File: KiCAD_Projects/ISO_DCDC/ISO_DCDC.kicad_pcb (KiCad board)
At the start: 2 copper layers, 100 x 120 mm, 74 parts, among them IC1 PC817, IC2 PC817, IC3 PC817, IC4 PC817, IC5 PC817, P1 CONN_01X01, P10 CONN_01X02, P11 CONN_01X02, P12 CONN_01X01, P13 CONN_01X04, P14 CONN_01X02, P15 CONN_01X02, P16 CONN_01X02, P19 CONN_01X01, P2 CONN_01X01, P20 CONN_01X01, P21 CONN_01X02, P22 CONN_01X01, P23 CONN_01X01, P25 CONN_01X01, P26 CONN_01X01, P3 CONN_01X01, P30 CONN_01X01, P4 CONN_01X02, P5 CONN_01X02, P6 CONN_01X04, P7 CONN_01X04, P8 CONN_01X01, P9 CONN_01X01, Q1 MOSFET_N, U1 V23076-D3001-D142, U2 V23076-D3001-D142, U3 V23076-D3001-D142

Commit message: no message
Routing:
- net +BATT: track 21.7 -> 53.5 mm
- net Net-(P30-Pad1): track 0.00 -> 10.0 mm
- net Net-(C3-Pad1): track 28.5 -> 30.7 mm
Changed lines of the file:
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@@
   (general
     (links 131)
-    (no_connects 3)
+    (no_connects 0)
     (area -0.075001 -0.075001 100.075001 120.075001)
     (thickness 1.6)
     (drawings 8)
-    (tracks 343)
+    (tracks 351)
     (zones 0)
     (modules 74)
@@
   )
   (setup
-    (last_trace_width 0.5)
+    (last_trace_width 0.25)
     (user_trace_width 0.5)
     (user_trace_width 1)
@@
   (segment (start 7 50.5) (end 7 43) (width 0.5) (layer B.Cu) (net 1))
   (segment (start 8.5 52) (end 7 50.5) (width 0.5) (layer B.Cu) (net 1))
+  (segment (start 20.8 59) (end 26.5 64.7) (width 0.25) (layer B.Cu) (net 2) (status 400000))
+  (segment (start 20 74) (end 14 80) (width 0.25) (layer B.Cu) (net 2) (status 800000))
+  (segment (start 25.5 74) (end 20 74) (width 0.25) (layer B.Cu) (net 2))
+  (segment (start 26.5 73) (end 25.5 74) (width 0.25) (layer B.Cu) (net 2))
+  (segment (start 26.5 64.7) (end 26.5 73) (width 0.25) (layer B.Cu) (net 2))
   (segment (start 35.1 45.3) (end 35.1 38.1) (width 3) (layer B.Cu) (net 2))
   (segment (start 35.1 38.1) (end 30 33) (width 3) (layer B.Cu) (net 2))
@@
   (segment (start 14 80) (end 14 85) (width 0.5) (layer B.Cu) (net 2))
   (segment (start 14 85) (end 13 86) (width 0.5) (layer B.Cu) (net 2))
+  (segment (start 26.4 25) (end 26.4 22.89972) (width 2) (layer B.Cu) (net 3) (status C00000))
+  (segment (start 26.4 22.89972) (end 26.49988 22.79984) (width 2) (layer B.Cu) (net 3) (status C00000))
   (segment (start 13 26.9) (end 15.6 26.9) (width 2) (layer B.Cu) (net 3))
   (segment (start 15.6 26.9) (end 16 26.5) (width 2) (layer B.Cu) (net 3))
@@
   (segment (start 27.5 73.5) (end 27.5 60) (width 0.5) (layer B.Cu) (net 32))
   (segment (start 25 76) (end 27.5 73.5) (width 0.5) (layer B.Cu) (net 32))
+  (segment (start 25 12.5) (end 35 12.5) (width 0.25) (layer B.Cu) (net 33) (status C00000))
   (segment (start 59.70016 38.19952) (end 59.70016 23.80048) (width 0.5) (layer B.Cu) (net 34))
   (segment (start 67.29984 99.34874) (end 82.26126 99.34874) (width 0.5) (layer B.Cu) (net 35))

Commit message: no message
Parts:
- R3, R4: footprint RP_KiCAD_Libs:0204_2f5 -> RP_KiCAD_Libs:C1608_WP; moved to B.Cu
- moved R4 5.02 mm to (36.0, 22.5)
- moved P19 2.50 mm to (17.5, 36.0)
- moved D3 2.06 mm to (25.0, 32.5)
- moved R3 1.12 mm to (40.5, 21.5), turned to 0 degrees
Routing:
- net +BATT: track 53.5 -> 64.0 mm
- net GNDPWR: track 354.3 -> 362.4 mm
- net Net-(DCDC1-Pad4): track 12.7 -> 8.59 mm
- net /15V: track 164.3 -> 165.9 mm
- net Net-(D3-Pad1): track 5.74 -> 6.45 mm

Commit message: no message
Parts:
- removed P16: CONN_01X02, RP_KiCAD_Connector:XA_2T
- removed P30: CONN_01X01, Heatsinks:16PB017_16.25.16
- added C11: 470p, RP_KiCAD_Libs:C1608_WP, B.Cu at (52.0, 15.0)
- added C2: 0.22u, RP_KiCAD_Libs:C1608_WP, B.Cu at (43.0, 10.0)
- added C8: 470p, RP_KiCAD_Libs:C1608_WP, B.Cu at (52.0, 13.0)
- added D7: DIODE, RP_KiCAD_Libs:C3216, B.Cu at (38.5, 19.0)
- added R10: 100k, RP_KiCAD_Libs:C1608_WP, B.Cu at (49.5, 14.0)
- added R13: R, RP_KiCAD_Libs:0204_2f5, F.Cu at (59.5, 19.5)
- added R14: R, RP_KiCAD_Libs:C1608_WP, B.Cu at (73.0, 13.5)
- D2: footprint Diodes_ThroughHole:Diode_DO-201AD_Horizontal_RM15 -> Diodes_SMD:POWER_DI5; moved to B.Cu
- DCDC1: value SI-8008HFE -> SI-8010Y; footprint TO_SOT_Packages_THT:Pentawatt_Neutral_Staggered_Verical_TO220-5-T05D -> TO_SOT_Packages_THT:TO-220_7_Vertical
- IC1, IC2, IC3, IC4, IC5: footprint Opto-Devices:Optocoupler_SMD_HandSoldering_KPC357_LTV35x_PC357_SingleChannel -> Housings_SOIC:SOIJ-4_5.3x5.3mm_Pitch1.27mm
- L1: footprint Choke_Toroid_ThroughHole:Choke_Toroid_horizontal_Diameter26mm -> Choke_Toroid_ThroughHole:Choke_Toroid_8.5x24mm_Vertical
- R19: moved to F.Cu
- R3: value R -> 15k
- R4: value R -> 1k
- moved D4 50.1 mm to (74.5, 18.5), turned to 270 degrees
- moved P10 42.0 mm to (77.5, 28.5)
- moved R7 41.6 mm to (77.5, 21.0), turned to 0 degrees
- moved C9 40.0 mm to (70.0, 28.5)
- moved DCDC2 36.8 mm to (48.8, 35.6)
- moved R8 32.9 mm to (66.0, 46.5), turned to 270 degrees
- moved P15 31.6 mm to (86.5, 28.5)
- moved R11 31.2 mm to (36.0, 70.5), turned to 270 degrees
- moved IC3 29.8 mm to (59.0, 68.5)
- moved Q1 29.8 mm to (32.5, 70.5)
- moved R21 29.5 mm to (66.0, 72.0)
- moved R19 29.3 mm to (34.0, 70.5)
- moved D5 27.8 mm to (68.5, 43.0), turned to 180 degrees
- moved C5 27.5 mm to (54.0, 8.50), turned to 180 degrees
- moved C3 25.8 mm to (24.5, 9.00), turned to 90 degrees
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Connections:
- DCDC1 pad 1: Net-(C3-Pad1) -> Net-(C2-Pad2)
- DCDC1 pad 3: GNDPWR -> Net-(C3-Pad1)
- DCDC1 pad 4: Net-(DCDC1-Pad4) -> GNDPWR
- DCDC1 pad 5: Net-(C5-Pad2) -> Net-(C8-Pad1)
- IC1 pad 2: /12V_CAN_GND -> /5V_GND
- IC2 pad 2: /5V_GND -> /12V_CAN_GND
- IC4 pad 2: Net-(IC4-Pad2) -> /5V_GND
- IC5 pad 1: /POWER_EN_HIGH -> Net-(IC5-Pad1)
- IC5 pad 3: Net-(IC5-Pad3) -> /5V_GND
- P13 pad 1: Net-(P13-Pad1) -> /5V_GND
- P13 pad 2: Net-(IC4-Pad2) -> /5V
- P13 pad 3: Net-(IC5-Pad4) -> Net-(P13-Pad3)
- P13 pad 4: Net-(IC5-Pad3) -> Net-(IC5-Pad4)
- P21 pad 1: /POWER_EN_HIGH -> Net-(P21-Pad1)
- P21 pad 2: Net-(P21-Pad2) -> /15V
- P4 pad 2: Net-(P21-Pad2) -> Net-(P21-Pad1)
- P5 pad 1: Net-(P21-Pad2) -> Net-(P21-Pad1)
- R22 pad 1: Net-(P13-Pad1) -> Net-(P13-Pad3)
- R3 pad 1: Net-(DCDC1-Pad4) -> Net-(DCDC1-Pad6)
- R4 pad 2: Net-(DCDC1-Pad4) -> Net-(DCDC1-Pad6)
- R6 pad 1: /5V -> /12V_CAN
- R9 pad 1: /12V_CAN -> /5V
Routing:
- net GNDPWR: track 362.4 -> 301.6 mm
- net /12V_RasPi: track 90.4 -> 47.6 mm
- net /12V_RasPi_GND: track 82.8 -> 47.2 mm
- net Net-(IC4-Pad2): track 26.5 -> 0.00 mm
- net /5V: track 55.3 -> 81.1 mm
- net Net-(P13-Pad1): track 25.5 -> 0.00 mm
- net Net-(IC5-Pad3): track 24.5 -> 0.00 mm
- net Net-(IC2-Pad3): track 30.9 -> 9.23 mm
- net Net-(C3-Pad1): track 30.7 -> 49.9 mm
- net +BATT: track 64.0 -> 47.2 mm
- net Net-(DCDC1-Pad6): track 0.00 -> 13.9 mm
- net Net-(IC3-Pad3): track 78.1 -> 64.7 mm
- net /POWER_EN_HIGH: track 262.5 -> 275.7 mm
- net Net-(IC5-Pad4): track 24.5 -> 13.0 mm
- net /12V_CAN: track 78.9 -> 89.8 mm
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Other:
- board size 100 x 120 mm -> 90 x 100 mm

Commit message: no message
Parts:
- added JP1: JUMPER, Pin_Headers:Pin_Header_Straight_1x02, F.Cu at (79.0, 40.5)
- added JP2: JUMPER, Pin_Headers:Pin_Header_Straight_1x02, F.Cu at (81.5, 55.5)
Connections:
- P6 pad 3: Net-(P6-Pad3) -> Net-(JP1-Pad1)
- P6 pad 4: Net-(P6-Pad4) -> Net-(JP2-Pad1)
- P7 pad 3: Net-(P6-Pad3) -> Net-(JP1-Pad2)
- P7 pad 4: Net-(P6-Pad4) -> Net-(JP2-Pad2)
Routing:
- net Net-(P6-Pad3): track 22.7 -> 0.00 mm, vias 2 -> 0
- net Net-(JP2-Pad2): track 0.00 -> 20.7 mm, vias 0 -> 2
- net Net-(P6-Pad4): track 20.6 -> 0.00 mm, vias 2 -> 0
- net Net-(JP1-Pad1): track 0.00 -> 18.4 mm, vias 0 -> 2
- net Net-(JP1-Pad2): track 0.00 -> 6.29 mm
- net Net-(JP2-Pad1): track 0.00 -> 5.83 mm

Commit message: 3Dデータ組み合わてテスト
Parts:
- DCDC4: footprint RP_KiCAD_Libs:MGS30 -> Converters_DCDC_ACDC:MGS30

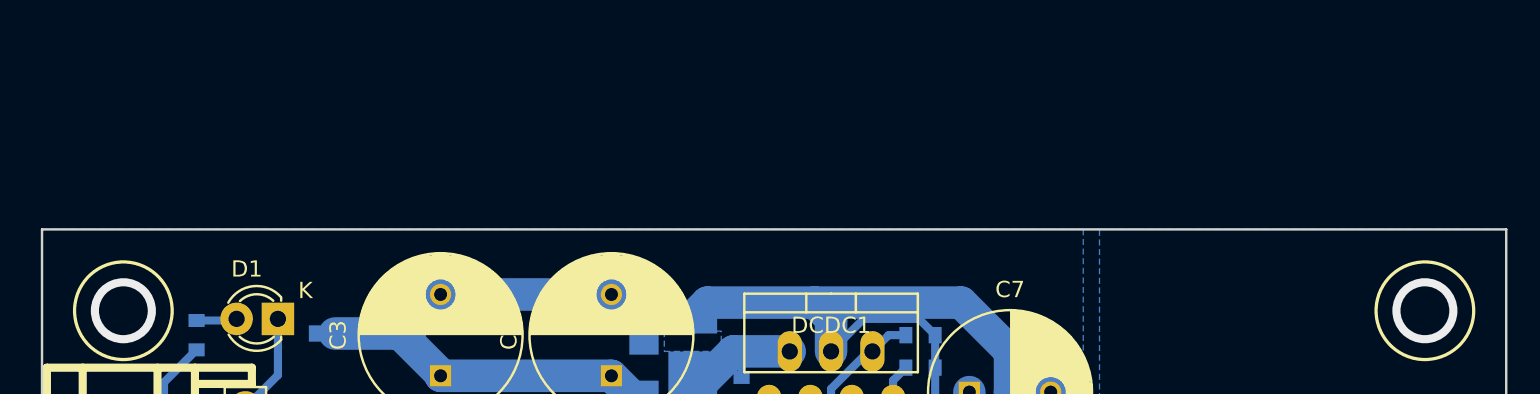
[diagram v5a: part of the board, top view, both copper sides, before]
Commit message: 4.0.5のライブラリを追加｡インダクタの3Dモジュール追加
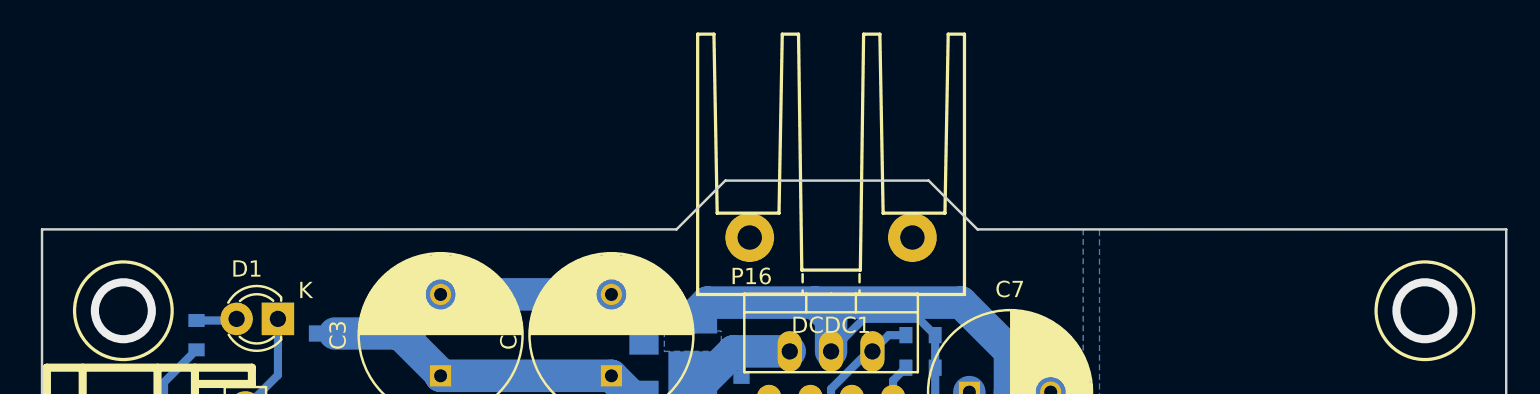
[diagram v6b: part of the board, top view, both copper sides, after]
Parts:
- added P16: TST, Heatsinks:16PB017_16.25.16, F.Cu at (48.5, 6.00)
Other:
- board size 90 x 100 mm -> 90 x 103 mm
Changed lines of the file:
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@@
-(kicad_pcb (version 4) (host pcbnew 4.0.4-stable)
+(kicad_pcb (version 4) (host pcbnew 4.0.5)
   (general
-    (links 144)
-    (no_connects 0)
+    (links 145)
+    (no_connects 1)
     (area -0.075001 -0.075001 90.075001 100.075001)
     (thickness 1.6)
-    (drawings 7)
+    (drawings 11)
     (tracks 437)
     (zones 0)
-    (modules 81)
-    (nets 50)
+    (modules 82)
+    (nets 51)
   )
   (page A4)
@@
   (net 48 "Net-(JP2-Pad1)")
   (net 49 "Net-(JP2-Pad2)")
+  (net 50 "Net-(P16-Pad1)")
   (net_class Default "これは標準のネット クラスです。"
     (clearance 0.2)
@@
     (add_net "Net-(JP2-Pad2)")
     (add_net "Net-(P13-Pad3)")
+    (add_net "Net-(P16-Pad1)")
     (add_net "Net-(P20-Pad1)")
     (add_net "Net-(P21-Pad1)")
@@
     )
   )
-  (module Choke_Toroid_ThroughHole:Choke_Toroid_8.5x24mm_Vertical (layer F.Cu)
-    (at 56 14 180)
-    (descr "Toroid, Coil, Choke,  8.5mm x 24mm, Vertical, Inductor, Drossel, Thruhole,")
-    (tags "Toroid, Coil, Choke,  8.5mm x 24mm, Vertical, Inductor, Drossel, Thruhole,")
-    (fp_text reference L1 (at 16.51 -10.16 180) (layer F.SilkS)
-      (effects (font (size 1 1) (thickness 0.15)))
-    )
-    (fp_text value "100uH 9A" (at 13 2 180) (layer F.Fab)
-      (effects (font (size 1 1) (thickness 0.15)))
-    )
-    (fp_line (start 0 0) (end 10 0) (layer F.SilkS) (width 0.2))
-    (fp_line (start 0 -7.5) (end 0 0) (layer F.SilkS) (width 0.2))
-    (fp_line (start 10 -7.5) (end 0 -7.5) (layer F.SilkS) (width 0.2))
-    (fp_line (start 13 0) (end 23 0) (layer F.SilkS) (width 0.2))
-    (fp_line (start 23 -7.5) (end 13 -7.5) (layer F.SilkS) (width 0.2))
-    (fp_line (start 23 -7.5) (end 23 0) (layer F.SilkS) (width 0.2))
-    (pad 1 thru_hole circle (at 11.5 0 180) (size 1.99898 1.99898) (drill 1) (layers *.Cu *.Mask F.SilkS)
-      (net 39 "Net-(C2-Pad1)"))
-    (pad 2 thru_hole circle (at 11.5 -7.5 180) (size 1.99898 1.99898) (drill 1) (layers *.Cu *.Mask F.SilkS)
-      (net 15 /15V))
-  )
   (module RP_KiCAD_Libs:0204_2f5 (layer F.Cu)
     (at 59.5 19.5 45)
@@
     )
   )
-  (gr_line (start 90 0) (end 0 0) (angle 90) (layer Edge.Cuts) (width 0.15))
+  (module Choke_Toroid_ThroughHole:Choke_Toroid_8.5x24mm_Vertical (layer F.Cu)
+    (at 56 14 180)
+    (descr "Toroid, Coil, Choke,  8.5mm x 24mm, Vertical, Inductor, Drossel, Thruhole,")
+    (tags "Toroid, Coil, Choke,  8.5mm x 24mm, Vertical, Inductor, Drossel, Thruhole,")
+    (fp_text reference L1 (at 16.51 -10.16 180) (layer F.SilkS)
+      (effects (font (size 1 1) (thickness 0.15)))
+    )
+    (fp_text value "100uH 9A" (at 13 2 180) (layer F.Fab)
+      (effects (font (size 1 1) (thickness 0.15)))
+    )
+    (fp_line (start 0 0) (end 10 0) (layer F.SilkS) (width 0.2))
+    (fp_line (start 0 -7.5) (end 0 0) (layer F.SilkS) (width 0.2))
+    (fp_line (start 10 -7.5) (end 0 -7.5) (layer F.SilkS) (width 0.2))
+    (fp_line (start 13 0) (end 23 0) (layer F.SilkS) (width 0.2))
+    (fp_line (start 23 -7.5) (end 13 -7.5) (layer F.SilkS) (width 0.2))
+    (fp_line (start 23 -7.5) (end 23 0) (layer F.SilkS) (width 0.2))
+    (pad 1 thru_hole circle (at 11.5 0 180) (size 1.99898 1.99898) (drill 1) (layers *.Cu *.Mask F.SilkS)
+      (net 39 "Net-(C2-Pad1)"))
+    (pad 2 thru_hole circle (at 11.5 -7.5 180) (size 1.99898 1.99898) (drill 1) (layers *.Cu *.Mask F.SilkS)
+      (net 15 /15V))
+    (model Choke_Toroid_ThroughHole.3dshapes/Choke_Toroid_11x25mm.wrl
+      (at (xyz 0.45 0.015 0.45))
+      (scale (xyz 0.37 0.37 0.37))
+      (rotate (xyz 90 0 0))
+    )
+  )
+  (module Heatsinks:16PB017_16.25.16 (layer F.Cu)
+    (at 48.5 6)
+    (fp_text reference P16 (at -4.9 -3.1) (layer F.SilkS)
+      (effects (font (size 1 1) (thickness 0.15)))
+    )
+    (fp_text value TST (at 4.9 -2.9) (layer F.Fab)
+      (effects (font (size 1 1) (thickness 0.15)))
+    )
+    (fp_line (start 1.8 -3.5) (end 2 -18) (layer F.SilkS) (width 0.2))
+    (fp_line (start -2 -18) (end -1.8 -3.5) (layer F.SilkS) (width 0.2))
+    (fp_line (start -7 -7) (end -3.2 -7) (layer F.SilkS) (width 0.2))
+    (fp_line (start 7 -7) (end 3.2 -7) (layer F.SilkS) (width 0.2))
+    (fp_line (start 7.2 -18) (end 7 -7) (layer F.SilkS) (width 0.2))
+    (fp_line (start 3 -18) (end 3.2 -7) (layer F.SilkS) (width 0.2))
+    (fp_line (start -3.2 -7) (end -3 -18) (layer F.SilkS) (width 0.2))
+    (fp_line (start -7.2 -18) (end -7 -7) (layer F.SilkS) (width 0.2))
+    (fp_line (start 2 -18) (end 3 -18) (layer F.SilkS) (width 0.2))
+    (fp_line (start -2 -18) (end -3 -18) (layer F.SilkS) (width 0.2))
+    (fp_line (start -1.8 -3.5) (end 1.8 -3.5) (layer F.SilkS) (width 0.2))
+    (fp_line (start 8.2 -18) (end 7.2 -18) (layer F.SilkS) (width 0.2))
+    (fp_line (start -8.2 -18) (end -7.2 -18) (layer F.SilkS) (width 0.2))
+    (fp_line (start -8.2 -2) (end -8.2 -18) (layer F.SilkS) (width 0.2))
+    (fp_line (start -8.2 -2) (end 8.2 -2) (layer F.SilkS) (width 0.2))
+    (fp_line (start 8.2 -2) (end 8.2 -18) (layer F.SilkS) (width 0.2))
+    (fp_line (start -1.75 -2.25) (end -1.75 -2) (layer F.SilkS) (width 0.15))
+    (fp_line (start 1.75 -2.25) (end 1.75 -2) (layer F.SilkS) (width 0.15))
+    (fp_line (start 1.75 -3.25) (end 1.75 -2.75) (layer F.SilkS) (width 0.15))
+    (fp_line (start -1.75 -3.25) (end -1.75 -2.75) (layer F.SilkS) (width 0.15))
+    (pad 1 thru_hole circle (at -5 -5.5) (size 3 3) (drill 1.5) (layers *.Cu *.Mask F.SilkS)
+      (net 50 "Net-(P16-Pad1)"))
+    (pad 1 thru_hole circle (at 5 -5.5) (size 3 3) (drill 1.5) (layers *.Cu *.Mask F.SilkS)
+      (net 50 "Net-(P16-Pad1)"))
+    (model Heatsinks/16PB017.wrl
+      (at (xyz 0 0.08 0))
+      (scale (xyz 3.9 3.9 3.9))
+      (rotate (xyz -90 0 0))
+    )
+  )
+  (gr_line (start 39 0) (end 0 0) (angle 90) (layer Edge.Cuts) (width 0.15))
+  (gr_line (start 57.5 0) (end 90 0) (angle 90) (layer Edge.Cuts) (width 0.15))
+  (gr_line (start 54.5 -3) (end 57.5 0) (angle 90) (layer Edge.Cuts) (width 0.15))
+  (gr_line (start 42 -3) (end 54.5 -3) (angle 90) (layer Edge.Cuts) (width 0.15))
+  (gr_line (start 39 0) (end 42 -3) (angle 90) (layer Edge.Cuts) (width 0.15))
   (gr_line (start 90 100) (end 90 0) (angle 90) (layer Edge.Cuts) (width 0.15))
   (gr_line (start 0 100) (end 90 100) (angle 90) (layer Edge.Cuts) (width 0.15))
@@
   (via (at 82 52.5) (size 1.5) (drill 0.8) (layers F.Cu B.Cu) (net 49))
   (segment (start 86.5 41) (end 85.5 41) (width 0.5) (layer B.Cu) (net 49))
-  (zone (net 1) (net_name GNDPWR) (layer B.Cu) (hatch edge 0.508)
-    (connect_pads yes (clearance 0.35))
-    (min_thickness 0.026)
-    (fill yes (arc_segments 16) (thermal_gap 0.508) (thermal_bridge_width 0.508))
-    (polygon
-      (pts
-        (xy 64 23) (xy 57.5 23) (xy 57.5 100) (xy 0 100) (xy 0 0)
-        (xy 64 0)
-      )
-    )
-    (polygon
-      (pts        (xy 5.5 29) (xy 5.5 91.5) (xy 10.5 96.5) (xy 33.5 96.5) (xy 33.5 19)
-        (xy 15.5 19)
-      )
-    )
-    (polygon
-      (pts        (xy 29.5 13.25) (xy 29.5 16.75) (xy 30.75 16.75) (xy 30.75 13.25)
-      )
-    )
-    (polygon
-      (pts        (xy 38.25 6.25) (xy 38.25 7.5) (xy 41.75 7.5) (xy 41.75 6.25)
-      )
-    )
-  )
   (zone (net 32) (net_name "Net-(D6-Pad1)") (layer B.Cu) (hatch edge 0.508)
     (connect_pads yes (clearance 0.4))
@@
       )
     )
+  )
+  (zone (net 1) (net_name GNDPWR) (layer B.Cu) (hatch edge 0.508)
+    (connect_pads yes (clearance 0.35))
+    (min_thickness 0.026)
+    (fill yes (arc_segments 16) (thermal_gap 0.508) (thermal_bridge_width 0.508))
+    (polygon
+      (pts
+        (xy 64 23) (xy 57.5 23) (xy 57.5 100) (xy 0 100) (xy 0 0)
+        (xy 39 0) (xy 42 -3) (xy 54.5 -3) (xy 57.5 0) (xy 64 0)
+      )
+    )
+    (polygon
+      (pts        (xy 5.5 29) (xy 5.5 91.5) (xy 10.5 96.5) (xy 33.5 96.5) (xy 33.5 19)
+        (xy 15.5 19)
+      )
+    )
+    (polygon
+      (pts        (xy 29.5 13.25) (xy 29.5 16.75) (xy 30.75 16.75) (xy 30.75 13.25)
+      )
+    )
+    (polygon
+      (pts        (xy 38.25 6.25) (xy 38.25 7.5) (xy 41.75 7.5) (xy 41.75 6.25)
+      )
+    )
